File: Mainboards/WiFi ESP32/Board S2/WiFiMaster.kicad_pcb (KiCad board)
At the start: 2 copper layers, 67.4 x 54.3 mm, 63 parts, among them IC1 MCP170X, IC2 NCP1117ST, IC3 ADuM142, IC4 ADuM142, IC5 ADuM142, IC6 IL0505, IC7 NCP1117ST, IC8 TPS61041, J1 USB_C_Receptacle_USB2.0, J2 Conn_02x05_Odd_Even, U1 ESP32-S3-MINI-1, X1 AKL18X-04W, X2 ALLSERIALMASTERM

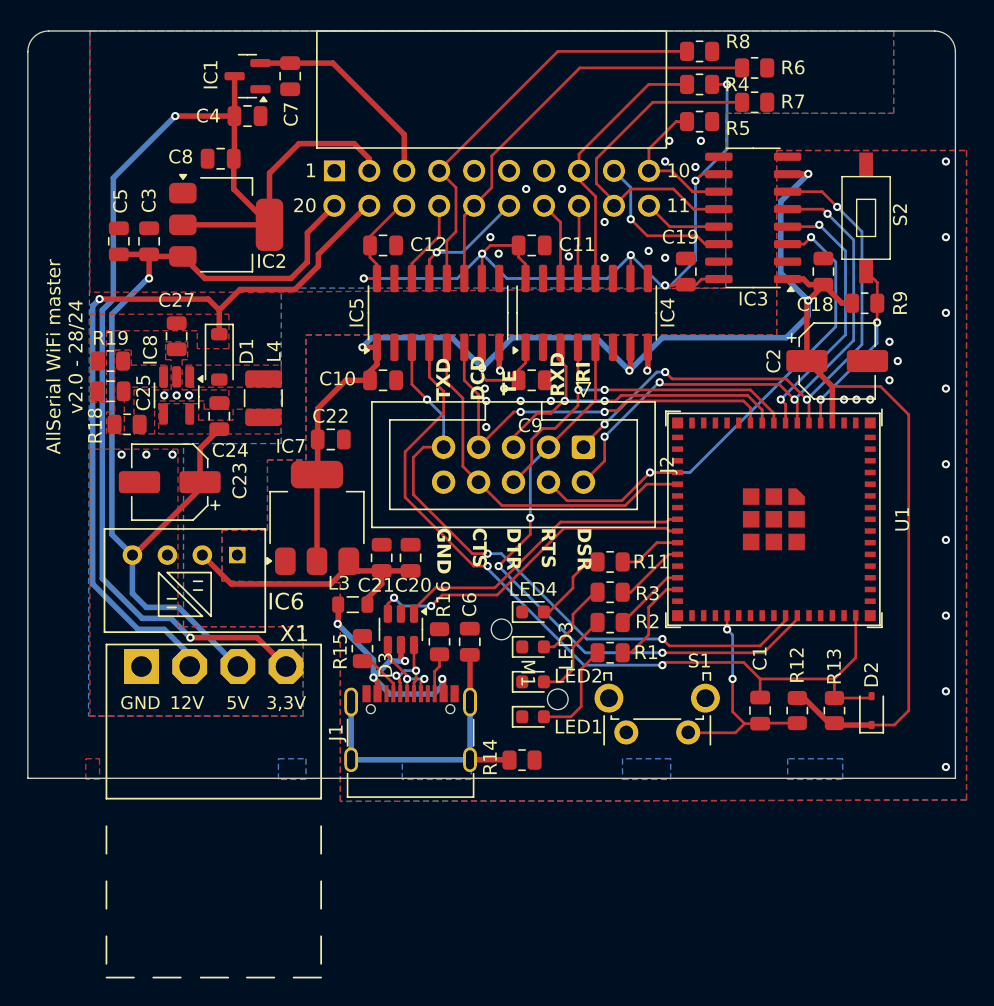
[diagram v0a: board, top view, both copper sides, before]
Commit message: Update AllSerial libraries
update projects
add slave project template
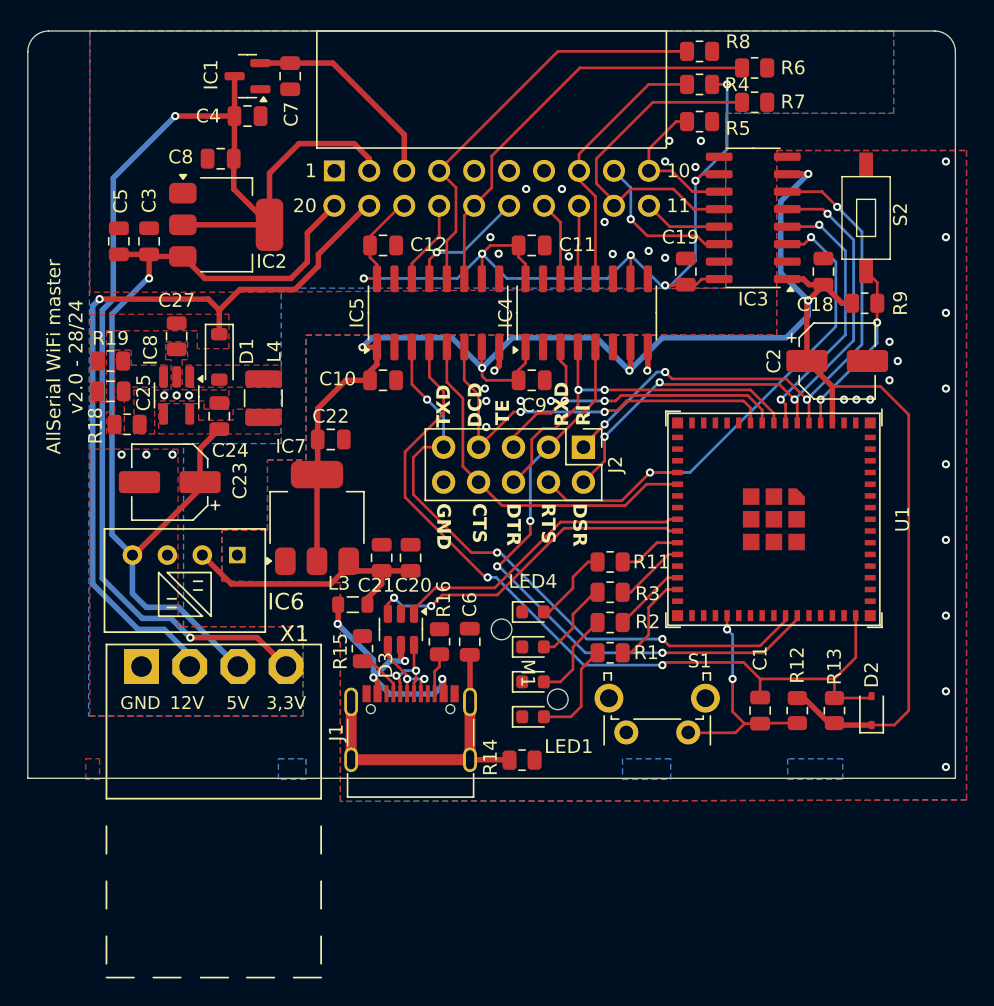
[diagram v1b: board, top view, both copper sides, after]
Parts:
- IC3, IC4, IC5: value ADuM142 -> ADuM142E1BRZ; footprint Package_SO:SOP-16_3.9x9.9mm_P1.27mm -> Package_SO:SOIC-16_3.9x9.9mm_P1.27mm
- J2: footprint Connector_IDC:IDC-Header_2x05_P2.54mm_Vertical -> Connector_PinHeader_2.54mm:PinHeader_2x05_P2.54mm_Vertical
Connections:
- net Net-(J1-SHIELD) renamed /SHLD
- IC4 pad 11: unconnected-(IC4E-INB-Pad11) -> GND2
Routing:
- net GND: track 3.52 -> 3.64 mm, vias 23 -> 22

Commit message: improve board/front links
clean up
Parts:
- S2: footprint WiFiMaster:SWITCH_BZCN_TSB008 -> Button_Switch_SMD:SW_SPST_CK_RS282G05A3
- moved R16 0.19 mm to (144.9, 122.0)
- moved C6 0.19 mm to (147.1, 122.0)
- moved D3 0.19 mm to (142.1, 121.1)
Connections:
- D3 pad 1: /USB_D- -> /USB_D+
- D3 pad 3: /USB_D+ -> /USB_D-
- J1 pad A6: Net-(D3-I/O2-Pad4) -> Net-(D3-I/O1-Pad6)
- J1 pad A7: Net-(D3-I/O1-Pad6) -> Net-(D3-I/O2-Pad4)
- J1 pad B6: Net-(D3-I/O2-Pad4) -> Net-(D3-I/O1-Pad6)
- J1 pad B7: Net-(D3-I/O1-Pad6) -> Net-(D3-I/O2-Pad4)
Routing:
- net /USB_D+: track 24.6 -> 22.3 mm, vias 2 -> 0
- net /USB_D-: track 22.2 -> 24.2 mm
- net Net-(D3-I/O2-Pad4): track 6.55 -> 6.96 mm, vias 2 -> 0

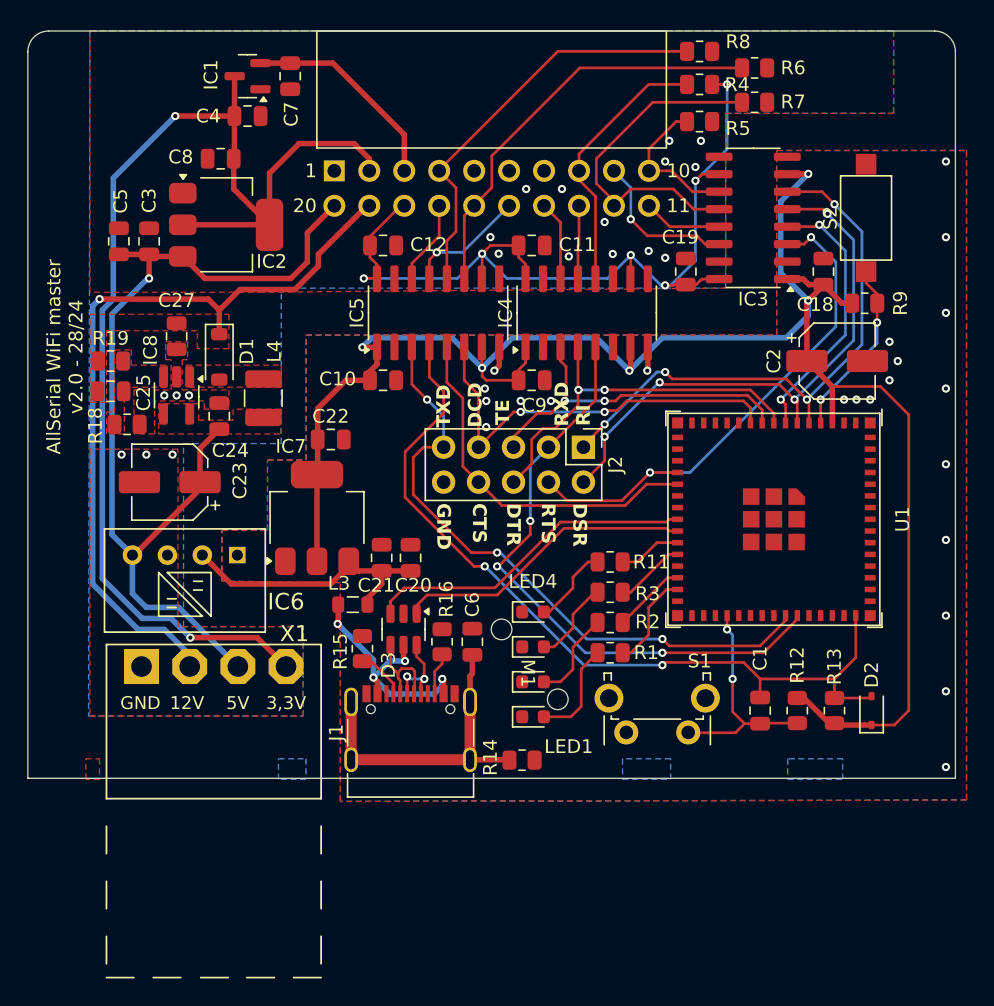
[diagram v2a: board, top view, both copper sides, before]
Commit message: Migrate to KiCad 9
Add eBus board
Add various libraries
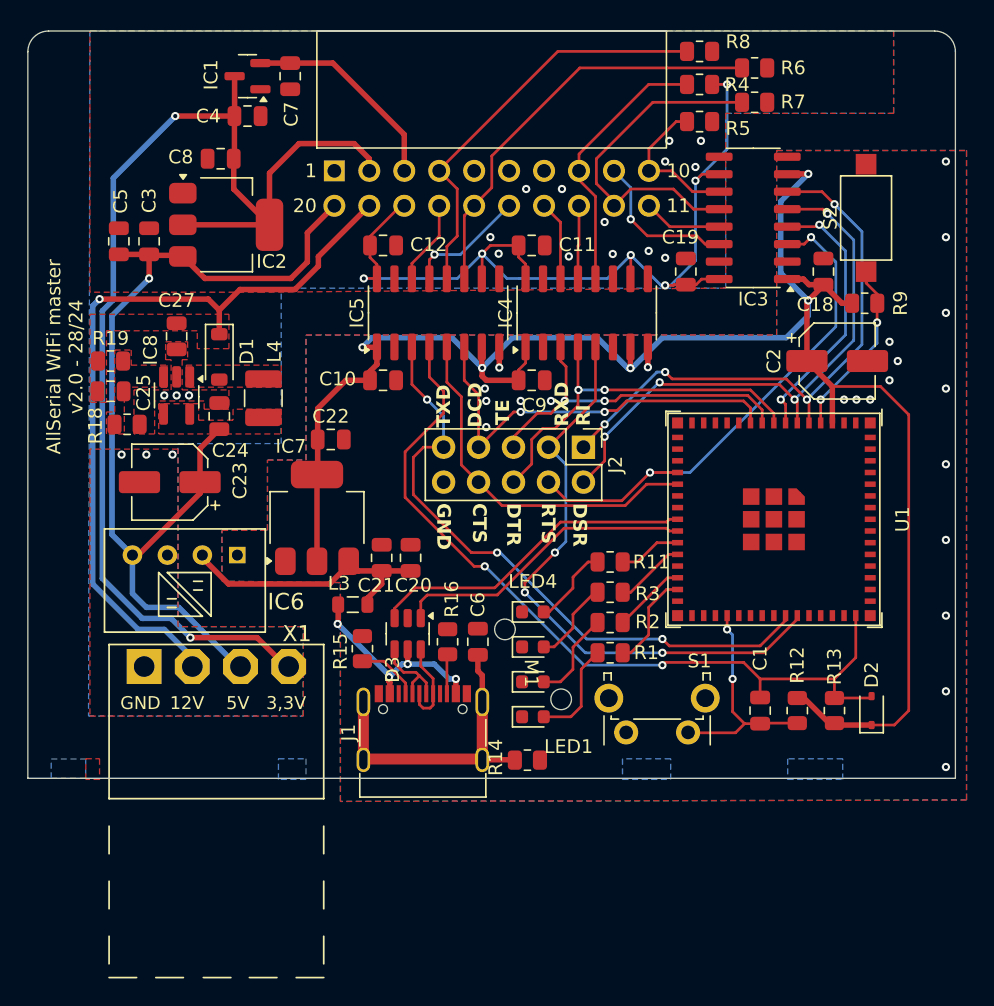
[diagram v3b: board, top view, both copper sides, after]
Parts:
- moved J1 0.89 mm to (143.5, 129.5)
- moved D3 0.44 mm to (142.4, 121.4)
- moved C6 0.40 mm to (147.5, 122.0)
- moved R16 0.40 mm to (145.3, 122.0)
- moved R14 0.39 mm to (151.1, 130.6)
- moved M1 0.24 mm to (151.5, 123.6)
- moved X1 0.19 mm to (128.5, 123.8)
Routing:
- net Net-(D3-VBUS): track 19.1 -> 15.9 mm
- net Net-(J1-CC1): track 3.67 -> 4.57 mm
- net /RXD_A: track 44.6 -> 43.9 mm
- net GND: track 3.64 -> 3.00 mm
- net +3.3V: track 133.3 -> 132.7 mm
- net Net-(D3-I/O1-Pad6): track 6.52 -> 6.71 mm, vias 2 -> 0

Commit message: improve AllSerial library
add assets for README
update README
cleanup
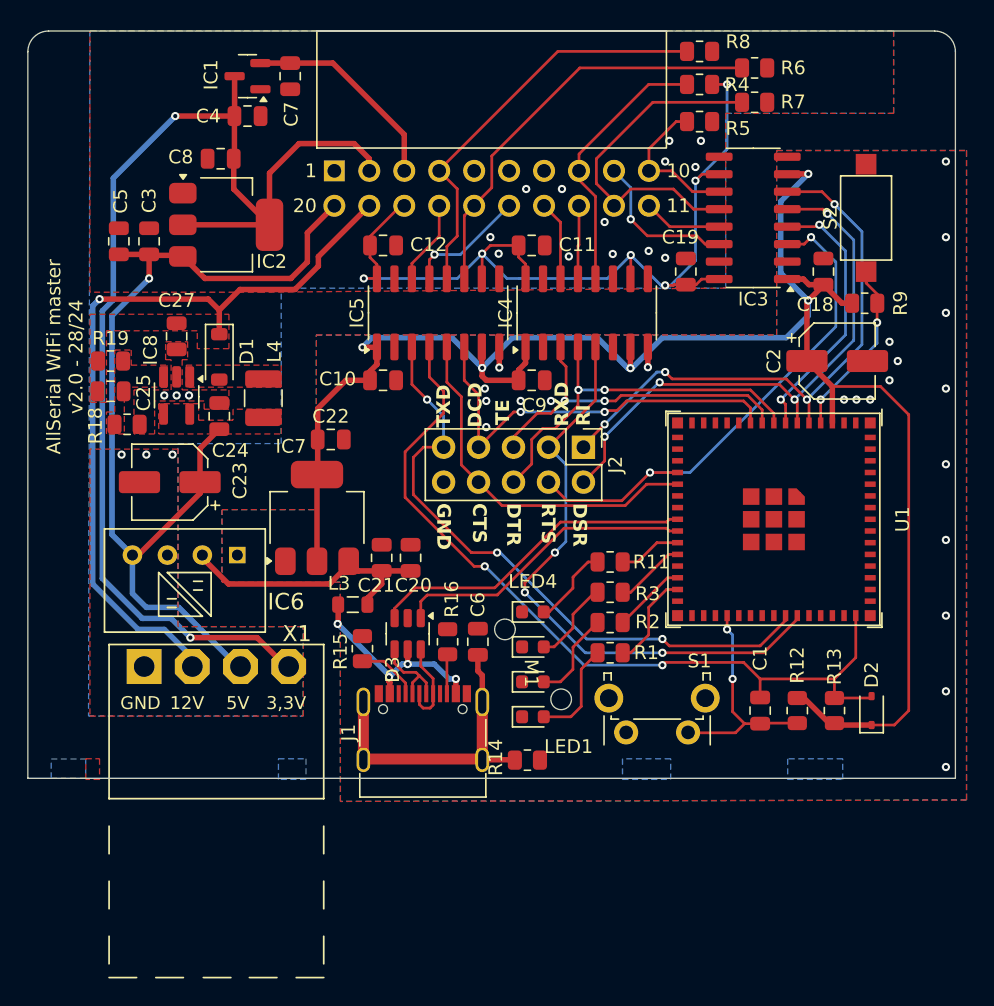
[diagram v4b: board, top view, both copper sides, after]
